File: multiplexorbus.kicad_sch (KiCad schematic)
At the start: 4 parts, among them U27 74LS138, U28 74LS138, U29 74LS137, U30 74LS137

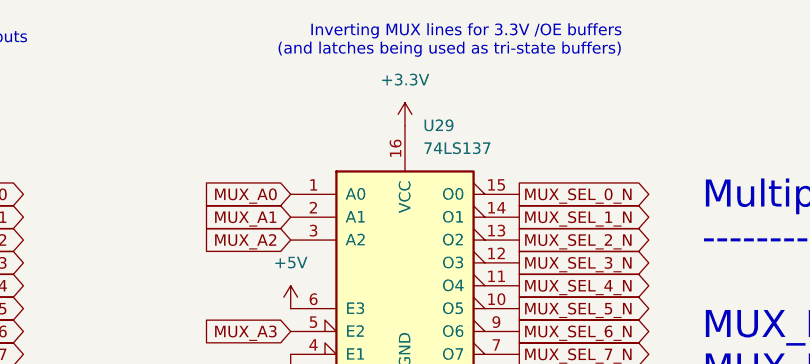
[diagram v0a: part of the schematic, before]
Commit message: more BOM parts cataloging
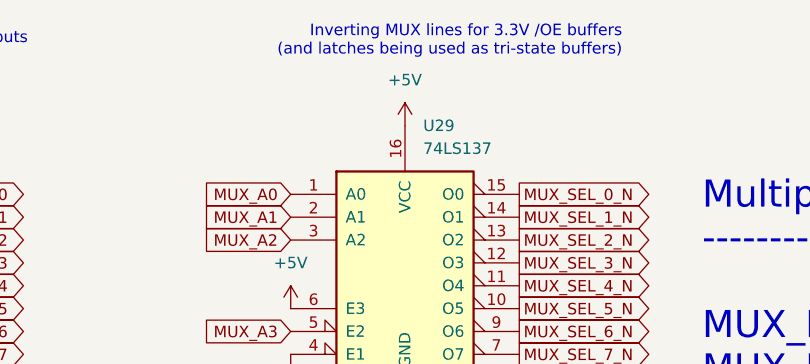
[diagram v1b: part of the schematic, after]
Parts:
- U29: footprint snapeda:DIP-16_LVC_Family -> snapeda:DIP-16_LS_Family
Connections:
- net +3V3: no longer U29.16 (VCC)
- net +5V: now also U29.16 (VCC)
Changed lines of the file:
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@@
       (effects (font (size 1.27 1.27)) (justify left))
     )
-    (property "Footprint" "snapeda:DIP-16_LVC_Family" (id 2) (at 120.65 40.64 0)
+    (property "Footprint" "snapeda:DIP-16_LS_Family" (id 2) (at 120.65 40.64 0)
       (effects (font (size 1.27 1.27)) hide)
     )
@@
     (pin "1")
   )
-  (symbol (lib_id "power:+3.3V") (at 120.65 25.4 0) (unit 1)
-    (in_bom yes) (on_board yes) (fields_autoplaced)
-    (property "Reference" "#PWR0231" (id 0) (at 120.65 29.21 0)
-      (effects (font (size 1.27 1.27)) hide)
-    )
-    (property "Value" "+3.3V" (id 1) (at 120.65 20.32 0))
-    (property "Footprint" "" (id 2) (at 120.65 25.4 0)
-      (effects (font (size 1.27 1.27)) hide)
-    )
-    (property "Datasheet" "" (id 3) (at 120.65 25.4 0)
-      (effects (font (size 1.27 1.27)) hide)
-    )
-    (pin "1")
-  )
   (symbol (lib_id "power:GND") (at 53.34 58.42 0) (unit 1)
     (in_bom yes) (on_board yes) (fields_autoplaced)
@@
       (effects (font (size 1.27 1.27)) hide)
     )
+    (pin "1")
+  )
+  (symbol (lib_id "power:+5V") (at 120.65 25.4 0) (unit 1)
+    (in_bom yes) (on_board yes) (fields_autoplaced)
+    (property "Reference" "#PWR?" (id 0) (at 120.65 29.21 0)
+      (effects (font (size 1.27 1.27)) hide)
+    )
+    (property "Value" "+5V" (id 1) (at 120.65 20.32 0))
+    (property "Footprint" "" (id 2) (at 120.65 25.4 0)
+      (effects (font (size 1.27 1.27)) hide)
+    )
+    (property "Datasheet" "" (id 3) (at 120.65 25.4 0)
+      (effects (font (size 1.27 1.27)) hide)
+    )

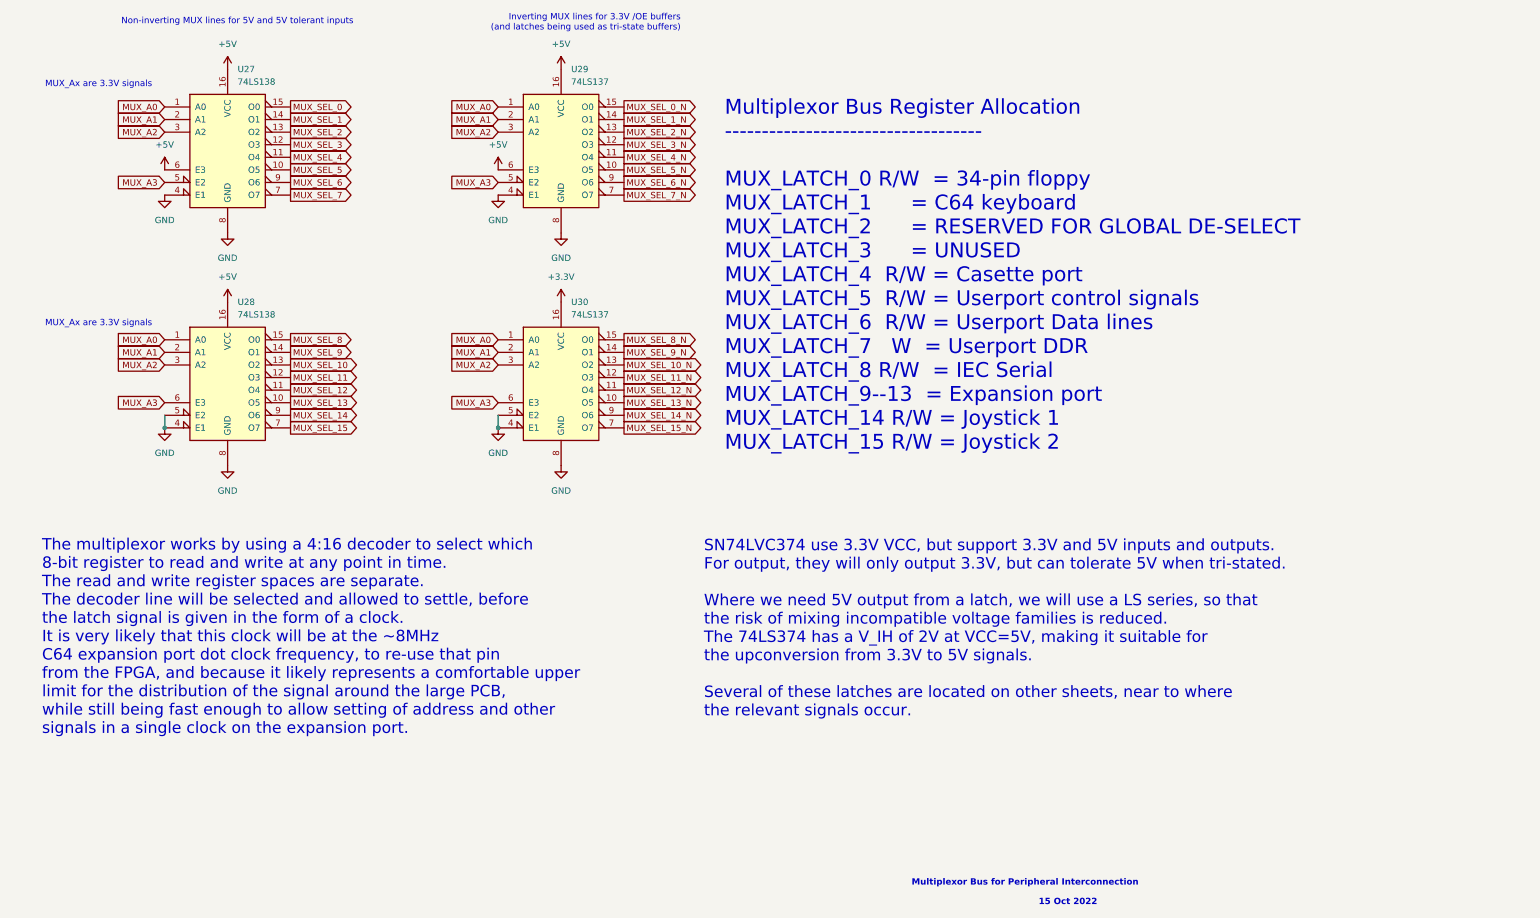
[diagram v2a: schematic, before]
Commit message: rework user port
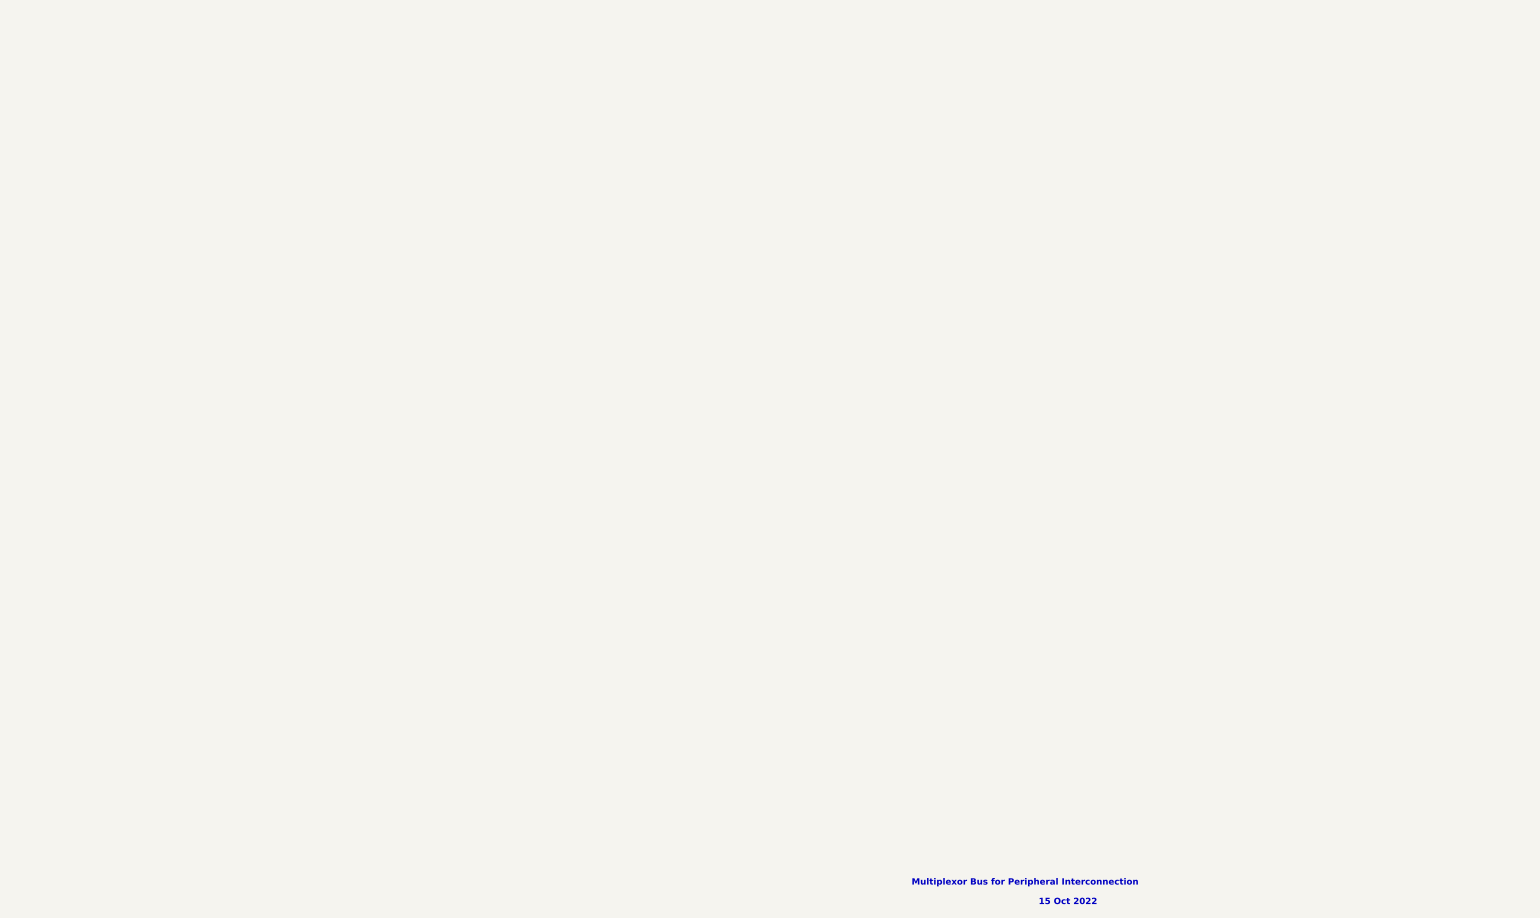
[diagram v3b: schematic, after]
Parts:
- removed U27, U28: 74LS138, snapeda:DIP-16_LS_Family, symbol 74xx:74LS138
- removed U29: 74LS137, snapeda:DIP-16_LS_Family, symbol 74xx:74LS138
- removed U30: 74LS137, snapeda:DIP-16_LVC_Family, symbol 74xx:74LS138
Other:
- note removed: "Inverting MUX lines for 3.3V /OE buffers (and latches being used as tri-state buffers)"
- note removed: "MUX_Ax are 3.3V signals"
- note removed: "Multiplexor Bus Register Allocation ----------------------------------- MUX_LATCH_0 R/W = 34-pin floppy MUX_LATCH_1 = C64 keyboard MUX_LATCH_2 = RESERVED FOR GLOBAL DE-SELECT MUX_LATCH_3 = UNUSED MUX_LATCH_4 R/W = Casette port MUX_LATCH_5 R/W = Userport control signals MUX_LATCH_6 R/W = Userport Data lines MUX_LATCH_7 W = Userport DDR MUX_LATCH_8 R/W = IEC Serial MUX_LATCH_9--13 = Expansion port 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"
- note removed: "Non-inverting MUX lines for 5V and 5V tolerant inputs"
- note removed: "SN74LVC374 use 3.3V VCC, but support 3.3V and 5V inputs and outputs. For output, they will only output 3.3V, but can tolerate 5V when tri-stated. Where we need 5V output from a latch, we will use a LS series, so that the risk of mixing incompatible voltage families is reduced. The 74LS374 has a V_IH of 2V at VCC=5V, making it suitable for the upconversion from 3.3V to 5V signals. Several of these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"
- note removed: "The multiplexor works by using a 4:16 decoder to select which 8-bit register to read and write at any point in time. The read and write register spaces are separate. The decoder line will be selected and allowed to settle, before the latch signal is given in the form of a clock. It is very likely that this clock will be at the ~8MHz C64 expansion port dot clock frequency, to re-use that pin from 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"

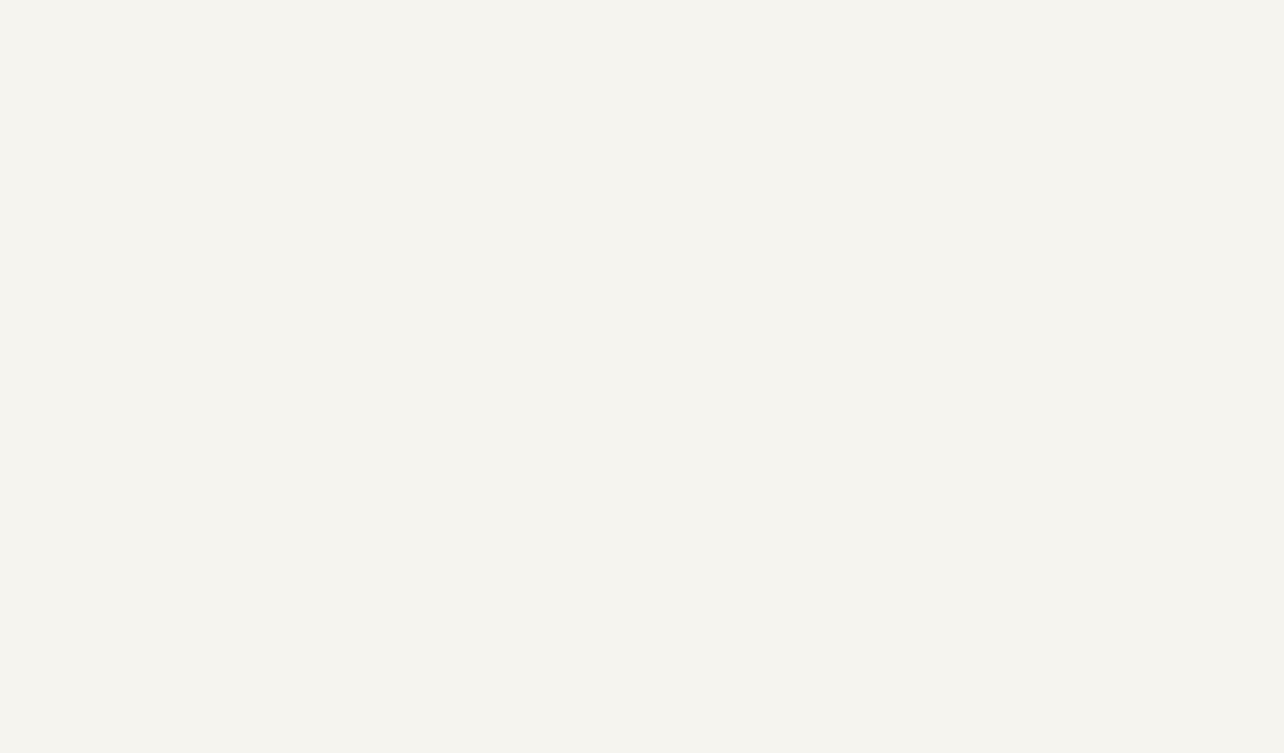
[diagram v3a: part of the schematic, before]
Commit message: reconnect everything and add PMOD and 34pin floppy connectors
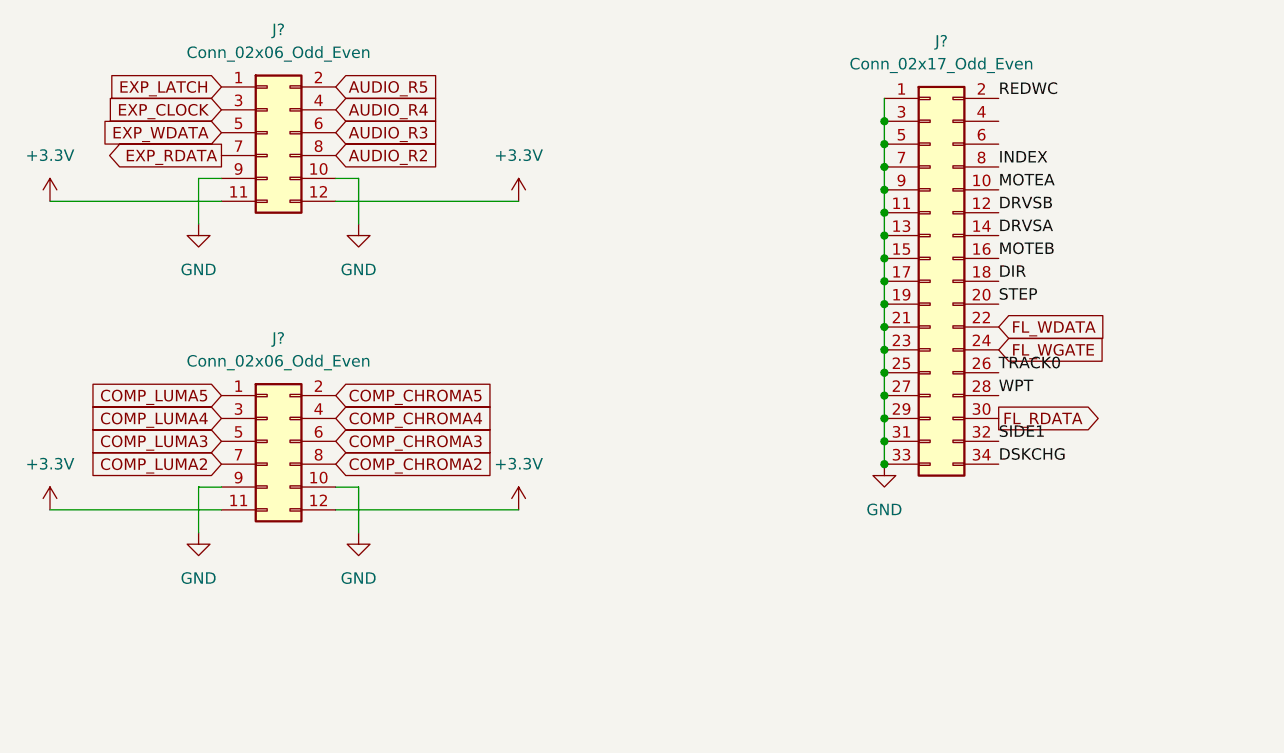
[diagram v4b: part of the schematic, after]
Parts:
- added J? (x2): Conn_02x06_Odd_Even, Connector_PinHeader_2.54mm:PinHeader_2x06_P2.54mm_Vertical, symbol Connector_Generic:Conn_02x06_Odd_Even
- added J?: Conn_02x17_Odd_Even, Connector_PinHeader_2.54mm:PinHeader_2x17_P2.54mm_Vertical, symbol Connector_Generic:Conn_02x17_Odd_Even
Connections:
- new net +3V3: J?.11 (Pin_11), J?.11 (Pin_11), J?.12 (Pin_12), J?.12 (Pin_12)
- new net AUDIO_R2: J?.8 (Pin_8)
- new net AUDIO_R3: J?.6 (Pin_6)
- new net AUDIO_R4: J?.4 (Pin_4)
- new net AUDIO_R5: J?.2 (Pin_2)
- new net COMP_CHROMA2: J?.8 (Pin_8)
- new net COMP_CHROMA3: J?.6 (Pin_6)
- new net COMP_CHROMA4: J?.4 (Pin_4)
- new net COMP_CHROMA5: J?.2 (Pin_2)
- new net COMP_LUMA2: J?.7 (Pin_7)
- new net COMP_LUMA3: J?.5 (Pin_5)
- new net COMP_LUMA4: J?.3 (Pin_3)
- new net COMP_LUMA5: J?.1 (Pin_1)
- new net DIR: J?.18 (Pin_18)
- new net DRVSA: J?.14 (Pin_14)
- new net DRVSB: J?.12 (Pin_12)
- new net DSKCHG: J?.34 (Pin_34)
- new net EXP_CLOCK: J?.3 (Pin_3)
- new net EXP_LATCH: J?.1 (Pin_1)
- new net EXP_RDATA: J?.7 (Pin_7)
- new net EXP_WDATA: J?.5 (Pin_5)
- new net FL_RDATA: J?.30 (Pin_30)
- new net FL_WDATA: J?.22 (Pin_22)
- new net FL_WGATE: J?.24 (Pin_24)
- new net GND: J?.1 (Pin_1), J?.10 (Pin_10), J?.10 (Pin_10), J?.11 (Pin_11), J?.13 (Pin_13), J?.15 (Pin_15), J?.17 (Pin_17), J?.19 (Pin_19), J?.21 (Pin_21), J?.23 (Pin_23), J?.25 (Pin_25), J?.27 (Pin_27), J?.29 (Pin_29), J?.3 (Pin_3), J?.31 (Pin_31), J?.33 (Pin_33), J?.5 (Pin_5), J?.7 (Pin_7), J?.9 (Pin_9), J?.9 (Pin_9), J?.9 (Pin_9)
- new net INDEX: J?.8 (Pin_8)
- new net MOTEA: J?.10 (Pin_10)
- new net MOTEB: J?.16 (Pin_16)
- new net REDWC: J?.2 (Pin_2)
- new net SIDE1: J?.32 (Pin_32)
- new net STEP: J?.20 (Pin_20)
- new net TRACK0: J?.26 (Pin_26)
- new net WPT: J?.28 (Pin_28)

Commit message: begin placing and routing
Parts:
- added J?: Conn_02x17_Odd_Even, Connector_PinHeader_2.54mm:PinHeader_2x17_P2.54mm_Vertical, symbol Connector_Generic:Conn_02x17_Odd_Even
- gave numbers to parts that had none: 3
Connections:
- net DIR: now also J?.18 (Pin_18)
- net DRVSA: now also J?.14 (Pin_14)
- net DRVSB: now also J?.12 (Pin_12)
- net DSKCHG: now also J?.34 (Pin_34)
- net FL_RDATA: now also J?.30 (Pin_30)
- net FL_WDATA: now also J?.22 (Pin_22)
- net FL_WGATE: now also J?.24 (Pin_24)
- net GND: now also J?.1 (Pin_1), J?.11 (Pin_11), J?.13 (Pin_13), J?.15 (Pin_15), J?.17 (Pin_17), J?.19 (Pin_19), J?.21 (Pin_21), J?.23 (Pin_23), J?.25 (Pin_25), J?.27 (Pin_27), J?.29 (Pin_29), J?.3 (Pin_3), J?.31 (Pin_31), J?.33 (Pin_33), J?.5 (Pin_5), J?.7 (Pin_7), J?.9 (Pin_9)
- net INDEX: now also J?.8 (Pin_8)
- net MOTEA: now also J?.10 (Pin_10)
- net MOTEB: now also J?.16 (Pin_16)
- net REDWC: now also J?.2 (Pin_2)
- net SIDE1: now also J?.32 (Pin_32)
- net STEP: now also J?.20 (Pin_20)
- net TRACK0: now also J?.26 (Pin_26)
- net WPT: now also J?.28 (Pin_28)

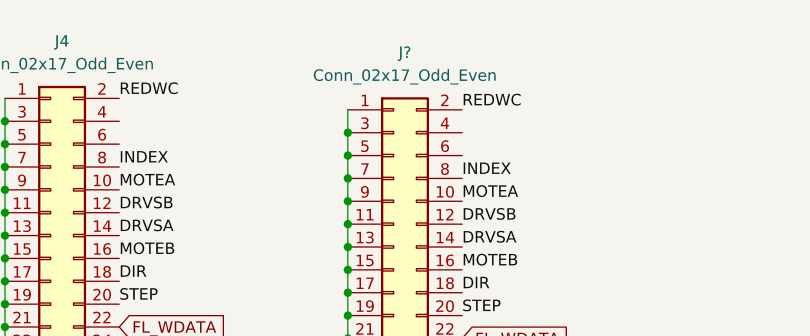
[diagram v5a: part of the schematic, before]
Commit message: fix U30 VCC and footprint
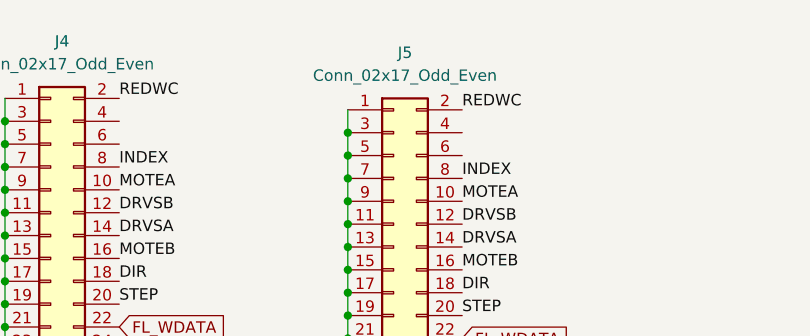
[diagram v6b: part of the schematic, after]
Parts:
- gave numbers to parts that had none: 1
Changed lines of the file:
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@@
   (symbol (lib_id "power:GND") (at 184.15 83.82 0) (unit 1)
     (in_bom yes) (on_board yes) (fields_autoplaced)
-    (property "Reference" "#PWR?" (id 0) (at 184.15 90.17 0)
+    (property "Reference" "#PWR0150" (id 0) (at 184.15 90.17 0)
       (effects (font (size 1.27 1.27)) hide)
     )
@@
   (symbol (lib_id "Connector_Generic:Conn_02x17_Odd_Even") (at 189.23 63.5 0) (unit 1)
     (in_bom yes) (on_board yes) (fields_autoplaced)
-    (property "Reference" "J?" (id 0) (at 190.5 36.83 0))
+    (property "Reference" "J5" (id 0) (at 190.5 36.83 0))
     (property "Value" "Conn_02x17_Odd_Even" (id 1) (at 190.5 39.37 0))
     (property "Footprint" "Connector_PinHeader_2.54mm:PinHeader_2x17_P2.54mm_Vertical" (id 2) (at 189.23 63.5 0)
